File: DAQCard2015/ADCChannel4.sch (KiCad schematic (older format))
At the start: 21 parts, among them U6 THS4524IDBTR, U7 AD9219

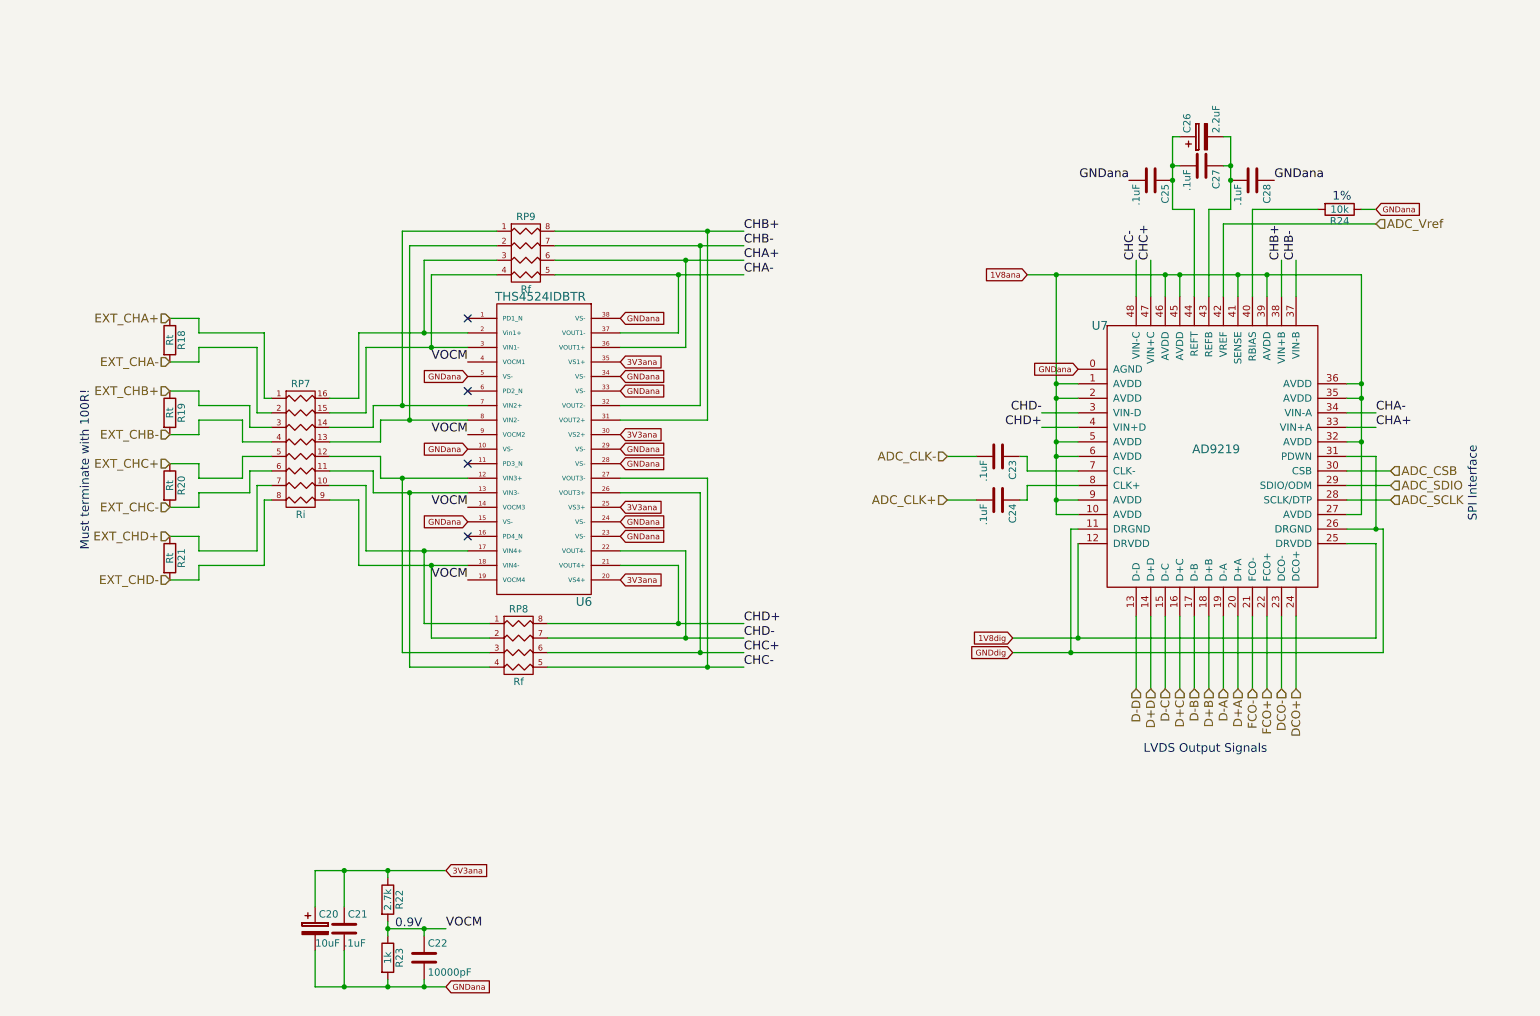
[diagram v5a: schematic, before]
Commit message: propogate previous changes to other channels and schematic
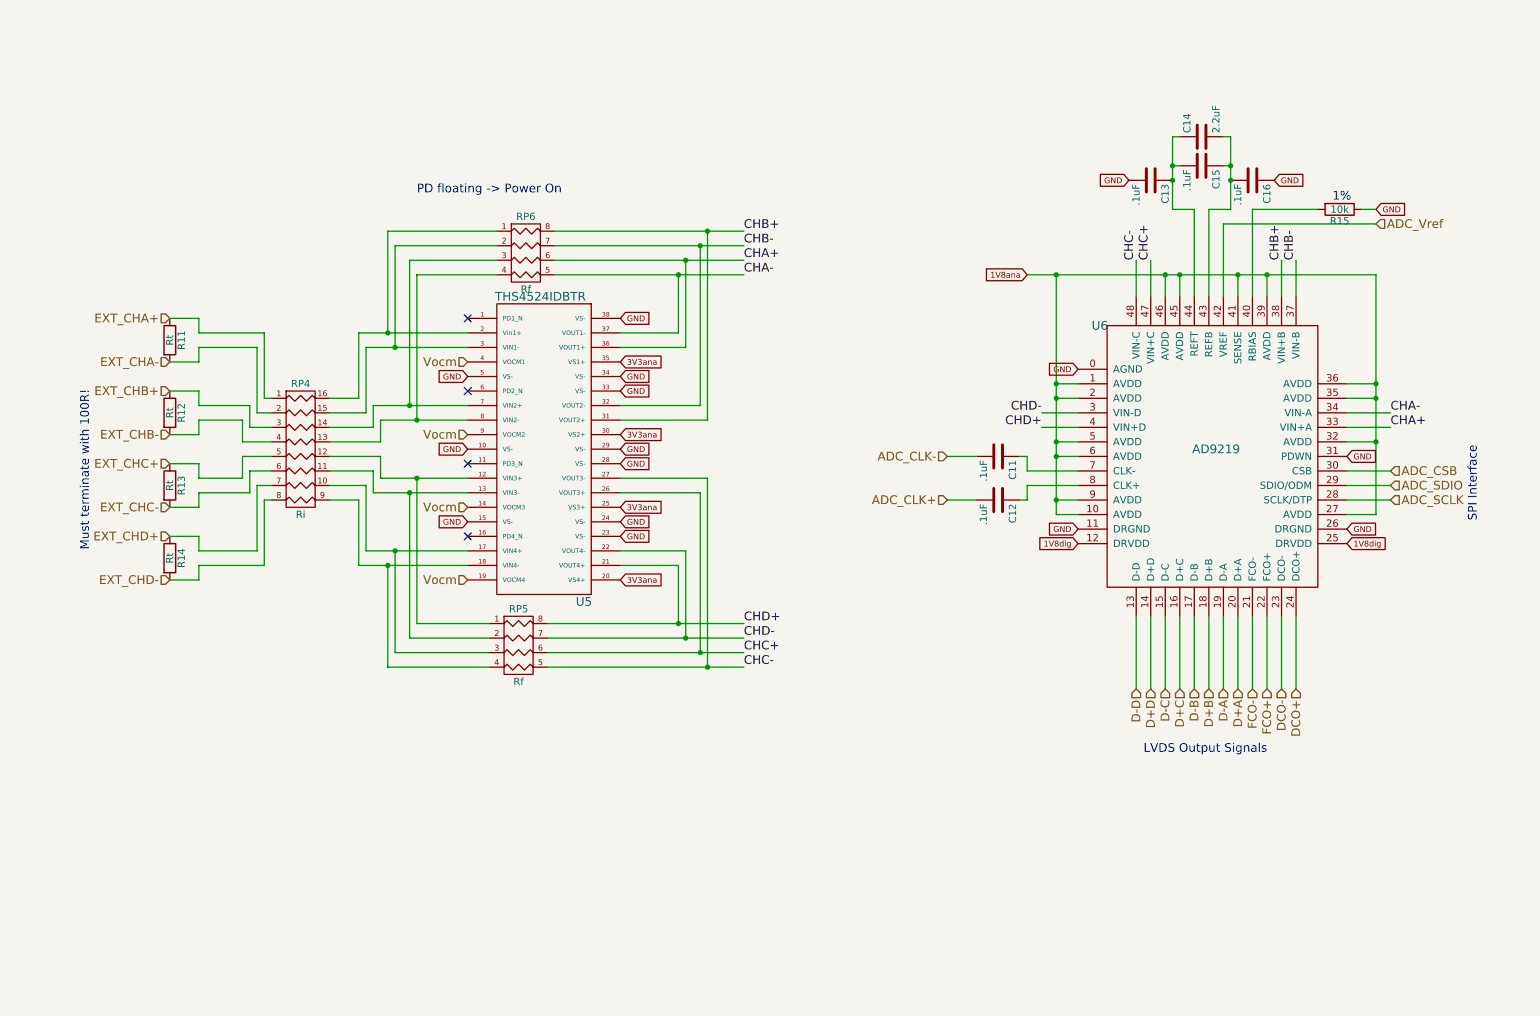
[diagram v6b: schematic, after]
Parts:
- removed C20: 10uF, Capacitors_SMD:C_0805, symbol CP
- removed C21, C23, C24, C25, C27, C28: .1uF, Capacitors_SMD:C_0603, symbol C
- removed C22: 10000pF, Capacitors_SMD:C_0603, symbol C
- removed C26: 2.2uF, Capacitors_SMD:C_0805, symbol CP
- removed R18, R19, R20, R21: Rt, Resistors_SMD:R_0603, symbol R
- removed R22: 2.7k, Resistors_SMD:R_0603, symbol R
- removed R23: 1k, Resistors_SMD:R_0603, symbol R
- removed R24: 10k, Resistors_SMD:R_0603, symbol R
- removed RP7: Ri, extras:R8_MNR18, symbol R_PACK8
- removed RP8, RP9: Rf, extras:R4-MNR04, symbol R_PACK4
- removed U6: THS4524IDBTR, Housings_SSOP:TSSOP-38_4.4x9.7mm_Pitch0.5mm, symbol THS4524IDBTR
- removed U7: AD9219, SMD_Packages:QFN-48-1EP, symbol AD9219
- added C11, C12, C13, C15, C16: .1uF, Capacitors_SMD:C_0603, symbol C
- added C14: 2.2uF, Capacitors_SMD:C_0805, symbol C
- added R11, R12, R13, R14: Rt, Resistors_SMD:R_0603, symbol R
- added R15: 10k, Resistors_SMD:R_0603, symbol R
- added RP4: Ri, extras:R8_MNR18, symbol R_PACK8
- added RP5, RP6: Rf, extras:R4-MNR04, symbol R_PACK4
- added U5: THS4524IDBTR, Housings_SSOP:TSSOP-38_4.4x9.7mm_Pitch0.5mm, symbol THS4524IDBTR
- added U6: AD9219, extras:QFN-48-1EP, symbol AD9219
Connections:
- net 1V8ana: now also U6.1 (AVDD), U6.10 (AVDD), U6.2 (AVDD), U6.27 (AVDD), U6.32 (AVDD), U6.35 (AVDD), U6.36 (AVDD), U6.39 (AVDD), U6.41 (SENSE), U6.45 (AVDD), U6.46 (AVDD), U6.5 (AVDD), U6.6 (AVDD), U6.9 (AVDD)
- net 1V8dig: now also U6.12 (DRVDD), U6.25 (DRVDD)
- net 3V3ana: now also U5.20 (VS4+), U5.25 (VS3+), U5.30 (VS2+), U5.35 (VS1+)
- net ADC_CLK+: now also C12.2
- net ADC_CLK-: now also C11.2
- net ADC_CSB: now also U6.30 (CSB)
- net ADC_SCLK: now also U6.28 (SCLK/DTP)
- net ADC_SDIO: now also U6.29 (SDIO/ODM)
- net ADC_Vref: now also U6.42 (VREF)
- net CHA+: now also RP6.6 (R3), U5.36 (VOUT1+), U6.33 (VIN+A)
- net CHA-: now also RP6.5 (R4), U5.37 (VOUT1-), U6.34 (VIN-A)
- net CHB+: now also RP6.8 (R1), U5.31 (VOUT2+), U6.38 (VIN+B)
- net CHB-: now also RP6.7 (R2), U5.32 (VOUT2-), U6.37 (VIN-B)
- net CHC+: now also RP5.6 (R3), U5.26 (VOUT3+), U6.47 (VIN+C)
- net CHC-: now also RP5.5 (R4), U5.27 (VOUT3-), U6.48 (VIN-C)
- net CHD+: now also RP5.8 (R1), U5.21 (VOUT4+), U6.4 (VIN+D)
- net CHD-: now also RP5.7 (R2), U5.22 (VOUT4-), U6.3 (VIN-D)
- net D+A: now also U6.20 (D+A)
- net D+B: now also U6.18 (D+B)
- net D+C: now also U6.16 (D+C)
- net D+D: now also U6.14 (D+D)
- net D-A: now also U6.19 (D-A)
- net D-B: now also U6.17 (D-B)
- net D-C: now also U6.15 (D-C)
- net D-D: now also U6.13 (D-D)
- net DCO+: now also U6.24 (DCO+)
- net DCO-: now also U6.23 (DCO-)
- net EXT_CHA+: now also R11.1, RP4.1 (P1)
- net EXT_CHA-: now also R11.2, RP4.2 (P2)
- net EXT_CHB+: now also R12.1, RP4.3 (P3)
- net EXT_CHB-: now also R12.2, RP4.4 (P4)
- net EXT_CHC+: now also R13.1, RP4.5 (P5)
- net EXT_CHC-: now also R13.2, RP4.6 (P6)
- net EXT_CHD+: now also R14.1, RP4.7 (P7)
- net EXT_CHD-: now also R14.2, RP4.8 (P8)
- net FCO+: now also U6.22 (FCO+)
- net FCO-: now also U6.21 (FCO-)
- new net: C12.1, U6.8 (CLK+)
- new net: C13.1, C14.1, C15.2, U6.44 (REFT)
- new net: C14.2, C15.1, C16.2, U6.43 (REFB)
- new net: RP4.16 (R1), RP6.1 (P1), U5.2 (Vin1+)
- new net: RP4.15 (R2), RP6.2 (P2), U5.3 (VIN1-)
- new net: RP4.14 (R3), RP6.3 (P3), U5.7 (VIN2+)
- new net: RP4.13 (R4), RP6.4 (P4), U5.8 (VIN2-)
- new net: R15.2, U6.40 (RBIAS)
- new net: C11.1, U6.7 (CLK-)
- new net: RP4.12 (R5), RP5.1 (P1), U5.12 (VIN3+)
- new net: RP4.11 (R6), RP5.2 (P2), U5.13 (VIN3-)
- new net: RP4.10 (R7), RP5.3 (P3), U5.17 (VIN4+)
- new net: RP4.9 (R8), RP5.4 (P4), U5.18 (VIN4-)
- new net GND: C13.2, C16.1, R15.1, U5.10 (VS-), U5.15 (VS-), U5.23 (VS-), U5.24 (VS-), U5.28 (VS-), U5.29 (VS-), U5.33 (VS-), U5.34 (VS-), U5.38 (VS-), U5.5 (VS-), U6.0 (AGND), U6.11 (DRGND), U6.26 (DRGND), U6.31 (PDWN)
- new net Vocm: U5.14 (VOCM3), U5.19 (VOCM4), U5.4 (VOCM1), U5.9 (VOCM2)
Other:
- note added: "PD floating -> Power On"
- note removed: "0.9V"

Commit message: Various updates to DAQ board focusing on power system
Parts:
- U5: footprint Housings_SSOP:TSSOP-38_4.4x9.7mm_Pitch0.5mm -> extras:TSSOP-38_4.4x9.7mm_Pitch0.5mm
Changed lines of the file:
@@
 F 0 "U5" H 4700 2750 60  0000 C CNN
 F 1 "THS4524IDBTR" H 4400 4850 60  0000 C CNN
-F 2 "Housings_SSOP:TSSOP-38_4.4x9.7mm_Pitch0.5mm" H 4600 3800 60  0001 C CNN
+F 2 "extras:TSSOP-38_4.4x9.7mm_Pitch0.5mm" H 4600 3800 60  0001 C CNN
 F 3 "" H 4600 3800 60  0000 C CNN
 	1    4400 3700

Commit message: Update to DAQ Board including adding an JTAG header and hooking up external clock and trigger
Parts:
- added C65: .1uF, Capacitors_SMD:C_0603, symbol C
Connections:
- net 3V3ana: now also C65.2
- net GND: now also C65.1
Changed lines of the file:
@@
 $Descr A4 11693 8268
 encoding utf-8
-Sheet 3 13
+Sheet 7 13
 Title ""
 Date ""
@@
 Text GLabel 8100 4150 0    40   Input ~ 0
 GND
+$Comp
+L C C65
+U 1 1 56064448
+P 4400 5500
+F 0 "C65" H 4425 5600 50  0000 L CNN
+F 1 ".1uF" H 4425 5400 50  0000 L CNN
+F 2 "Capacitors_SMD:C_0603" H 4438 5350 30  0001 C CNN
+F 3 "" H 4400 5500 60  0000 C CNN
+	1    4400 5500
+	0    1    1    0
+$EndComp
+Text GLabel 4250 5500 0    40   Input ~ 0
+3V3ana
+Text GLabel 4550 5500 2    40   Input ~ 0
+GND
 $EndSCHEMATC
